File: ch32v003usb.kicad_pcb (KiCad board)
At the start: 2 copper layers, 15.2 x 20.3 mm, 29 parts, among them J1 USB_B_Micro, U1 CH32V003F4U6, U2 MIC5365-3.3YC5

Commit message: routing about done
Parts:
- renumbered R4 to R3, R3 to R4
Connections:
- R3 pad 1: /USB_D+ -> /USB_D-
- R3 pad 2: /USB_D+ -> /USB_D-
- R4 pad 1: /USB_D- -> /USB_D+
- R4 pad 2: /USB_D- -> /USB_D+
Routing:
- net GND: track 24.1 -> 22.8 mm, vias 3 -> 4
- added copper zone on B.Cu, net GND
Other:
- outline, holes or cut-outs redrawn

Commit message: ground plane
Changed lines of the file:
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@@
     (effects (font (size 0.8 0.8) (thickness 0.12)))
   )
-  (segment (start 102.2 80.7) (end 104.2 78.7) (width 0.3) (layer "F.Cu") (net 1))
+  (segment (start 105.74 73.66) (end 106.35 73.66) (width 0.3) (layer "F.Cu") (net 1))
   (segment (start 98.6 88.6) (end 99.1 88.6) (width 0.2) (layer "F.Cu") (net 1))
   (segment (start 99.1 88.6) (end 99.2 88.5) (width 0.2) (layer "F.Cu") (net 1))
   (segment (start 103.125 82.7) (end 103.125 83.675) (width 0.3) (layer "F.Cu") (net 1))
-  (segment (start 103.125 82.7) (end 103.1 82.7) (width 0.2) (layer "F.Cu") (net 1))
   (segment (start 99.2 88.5) (end 99.2 88.06) (width 0.2) (layer "F.Cu") (net 1))
-  (segment (start 104.2 78.7) (end 104.2 75.81) (width 0.3) (layer "F.Cu") (net 1))
-  (segment (start 104.2 75.81) (end 106.35 73.66) (width 0.3) (layer "F.Cu") (net 1))
   (segment (start 100.6 81.2) (end 101.7 81.2) (width 0.3) (layer "F.Cu") (net 1))
   (segment (start 102.2 80.7) (end 103.125 81.625) (width 0.3) (layer "F.Cu") (net 1))
+  (segment (start 104.5 74.9) (end 105.74 73.66) (width 0.3) (layer "F.Cu") (net 1))
   (segment (start 103.125 83.675) (end 103.1 83.7) (width 0.3) (layer "F.Cu") (net 1))
   (segment (start 103.125 81.625) (end 103.125 82.7) (width 0.3) (layer "F.Cu") (net 1))
+  (segment (start 102.2 80.7) (end 104.5 78.4) (width 0.3) (layer "F.Cu") (net 1))
   (segment (start 101.7 81.2) (end 102.2 80.7) (width 0.3) (layer "F.Cu") (net 1))
+  (segment (start 104.5 78.4) (end 104.5 74.9) (width 0.3) (layer "F.Cu") (net 1))
   (via (at 98.6 88.6) (size 0.8) (drill 0.4) (layers "F.Cu" "B.Cu") (net 1))
   (via (at 103.1 83.7) (size 0.8) (drill 0.4) (layers "F.Cu" "B.Cu") (net 1))
@@
   (via (at 96.7 80.8) (size 0.8) (drill 0.4) (layers "F.Cu" "B.Cu") (net 2))
   (via (at 98.3 77.8) (size 0.8) (drill 0.4) (layers "F.Cu" "B.Cu") (net 2))
+  (segment (start 93.65 73.66) (end 94.26 73.66) (width 0.3) (layer "F.Cu") (net 3))
   (segment (start 99.3 79.3) (end 99.3 78.6) (width 0.3) (layer "F.Cu") (net 3))
-  (segment (start 94.26 73.66) (end 96.1 75.5) (width 0.3) (layer "F.Cu") (net 3))
+  (segment (start 94.26 73.66) (end 95.4 74.8) (width 0.3) (layer "F.Cu") (net 3))
   (segment (start 101 78.6) (end 100.6 78.6) (width 0.3) (layer "F.Cu") (net 3))
-  (segment (start 96.1 77.625) (end 97.7 79.225) (width 0.3) (layer "F.Cu") (net 3))
   (segment (start 101.3 78.3) (end 101 78.6) (width 0.3) (layer "F.Cu") (net 3))
   (segment (start 99.3 78.6) (end 98.325 78.6) (width 0.3) (layer "F.Cu") (net 3))
-  (segment (start 96.1 75.5) (end 96.1 77.625) (width 0.3) (layer "F.Cu") (net 3))
+  (segment (start 95.4 74.8) (end 95.4 76.925) (width 0.3) (layer "F.Cu") (net 3))
   (segment (start 99.3 78.6) (end 100.6 78.6) (width 0.3) (layer "F.Cu") (net 3))
   (segment (start 98.325 78.6) (end 97.7 79.225) (width 0.3) (layer "F.Cu") (net 3))
   (segment (start 100.6 78.6) (end 100.6 79.3) (width 0.3) (layer "F.Cu") (net 3))
+  (segment (start 95.4 76.925) (end 97.7 79.225) (width 0.3) (layer "F.Cu") (net 3))
   (segment (start 101.3 76.485) (end 101.3 78.3) (width 0.3) (layer "F.Cu") (net 3))
-  (segment (start 93.65 73.66) (end 94.26 73.66) (width 0.3) (layer "F.Cu") (net 3))
   (segment (start 100.5 77.8) (end 100.65 77.65) (width 0.2) (layer "F.Cu") (net 4))
+  (segment (start 100 83.1) (end 100 85.16) (width 0.2) (layer "F.Cu") (net 4))
   (segment (start 100.4 82.7) (end 101.475 82.7) (width 0.2) (layer "F.Cu") (net 4))
   (segment (start 100.65 77.65) (end 100.65 76.485) (width 0.2) (layer "F.Cu") (net 4))
-  (segment (start 100 83.1) (end 100 85.16) (width 0.2) (layer "F.Cu") (net 4))
   (segment (start 100.4 82.7) (end 100 83.1) (width 0.2) (layer "F.Cu") (net 4))
   (segment (start 99.025 82.7) (end 100.4 82.7) (width 0.2) (layer "F.Cu") (net 4))
@@
   (via (at 99.5 77.8) (size 0.8) (drill 0.4) (layers "F.Cu" "B.Cu") (net 5))
   (via (at 100.7 83.7) (size 0.8) (drill 0.4) (layers "F.Cu" "B.Cu") (net 5))
-  (segment (start 100 83.7) (end 100.7 83.7) (width 0.2) (layer "B.Cu") (net 5))
-  (segment (start 99.5 77.8) (end 99.5 83.2) (width 0.2) (layer "B.Cu") (net 5))
-  (segment (start 99.5 83.2) (end 100 83.7) (width 0.2) (layer "B.Cu") (net 5))
+  (segment (start 100 83.5) (end 100.5 83.5) (width 0.2) (layer "B.Cu") (net 5))
+  (segment (start 99.5 83) (end 100 83.5) (width 0.2) (layer "B.Cu") (net 5))
+  (segment (start 99.5 77.8) (end 99.5 83) (width 0.2) (layer "B.Cu") (net 5))
+  (segment (start 100.5 83.5) (end 100.7 83.7) (width 0.2) (layer "B.Cu") (net 5))
   (segment (start 93.65 81.28) (end 95.07 82.7) (width 0.2) (layer "F.Cu") (net 7))
   (segment (start 95.07 82.7) (end 97.375 82.7) (width 0.2) (layer "F.Cu") (net 7))
@@
       )
     )
+  )
+  (zone (net 0) (net_name "") (layers "B.Cu" "Edge.Cuts") (hatch edge 0.5)
+    (connect_pads (clearance 0))
+    (min_thickness 0.25) (filled_areas_thickness no)
+    (keepout (tracks allowed) (vias allowed) (pads allowed) (copperpour not_allowed) (footprints allowed))
+    (fill (thermal_gap 0.5) (thermal_bridge_width 0.5))
+    (polygon
+      (pts
+        (xy 98.4 79.2)
+        (xy 101.4 79.2)
+        (xy 101.4 81.6)
+        (xy 98.4 81.6)
+      )
+    )

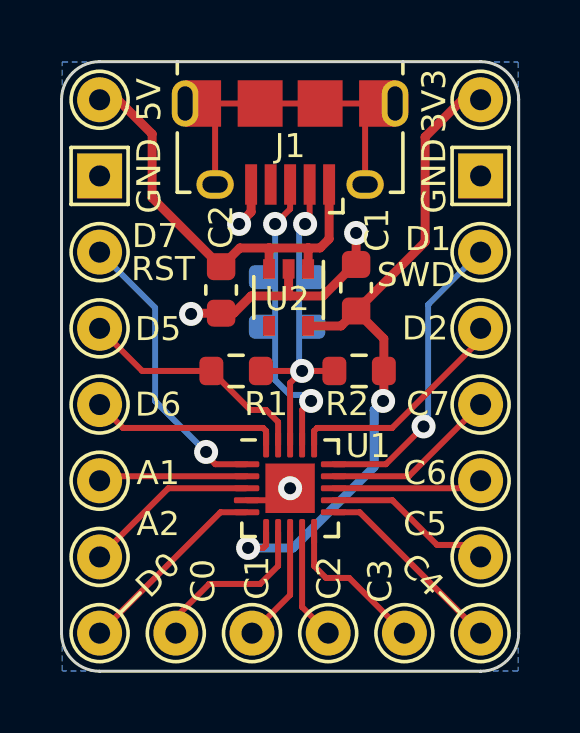
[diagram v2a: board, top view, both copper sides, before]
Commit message: Silkscreen updates
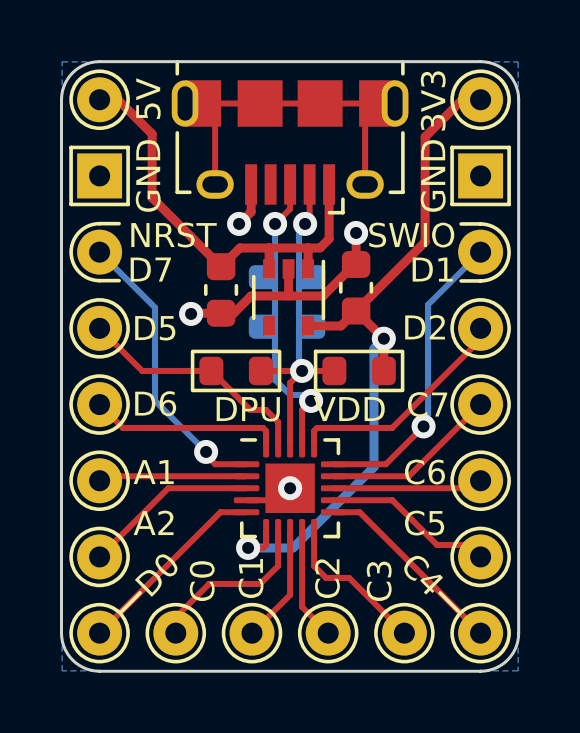
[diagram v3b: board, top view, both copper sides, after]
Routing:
- net VDD: track 23.0 -> 24.1 mm
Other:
- board text added: "CH32V003"
- board text added: "DPU"
- board text added: "NRST"
- board text added: "SWIO"
- board text added: "VDD"
- board text removed: "RST"
- board text removed: "SWD"

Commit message: rounding
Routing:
- net GND: track 22.8 -> 21.9 mm
- net Net-(J1-VBUS): track 14.8 -> 15.6 mm
